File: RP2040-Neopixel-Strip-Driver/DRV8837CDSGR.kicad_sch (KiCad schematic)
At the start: 1 part

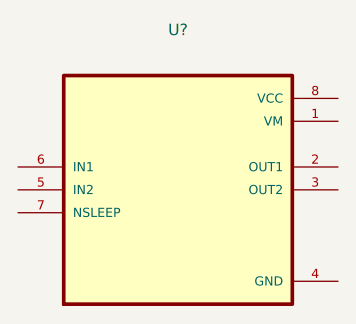
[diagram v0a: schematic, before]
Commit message: Moved USB and 3.3V Regulator from RP2040 to Power Sheet
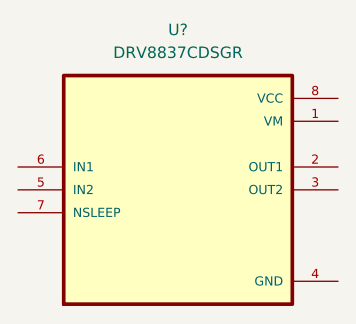
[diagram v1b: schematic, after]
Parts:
- U?: value (none) -> DRV8837CDSGR; footprint (none) -> SON50P200X200X80-9N
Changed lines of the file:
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@@
     (in_bom yes) (on_board yes) (fields_autoplaced)
     (property "Reference" "U?" (id 0) (at 142.24 81.28 0))
-    (property "Value" "" (id 1) (at 142.24 83.82 0))
-    (property "Footprint" "" (id 2) (at 142.24 99.06 0)
+    (property "Value" "DRV8837CDSGR" (id 1) (at 142.24 83.82 0))
+    (property "Footprint" "SON50P200X200X80-9N" (id 2) (at 142.24 99.06 0)
       (effects (font (size 1.27 1.27)) (justify left bottom) hide)
     )
